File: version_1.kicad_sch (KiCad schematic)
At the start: 2 parts, among them U1 74AHC595, U10 74AHC595

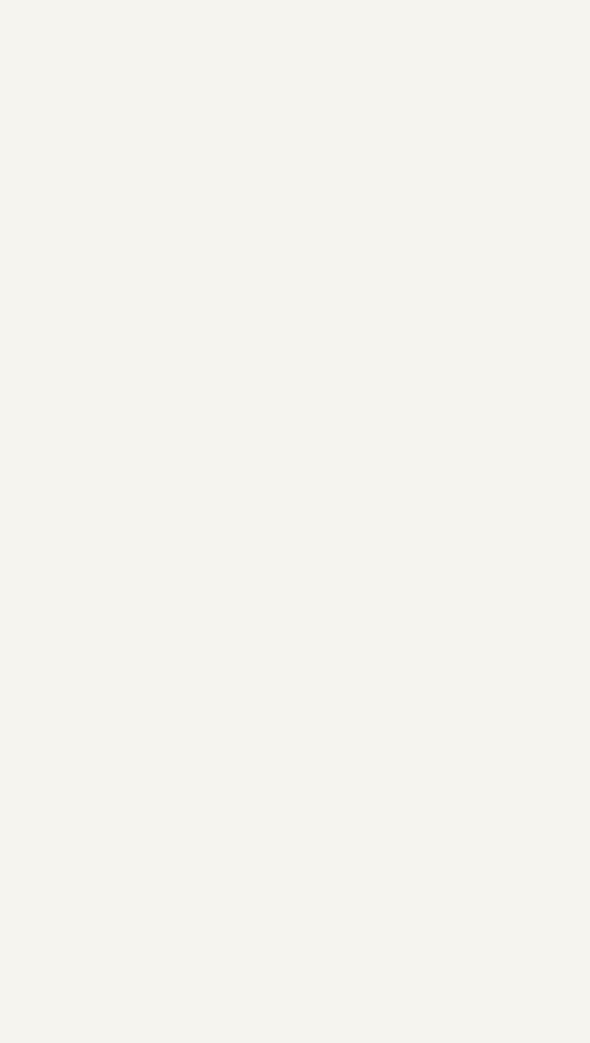
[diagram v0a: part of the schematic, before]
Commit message: mostek H, serva, SMPS
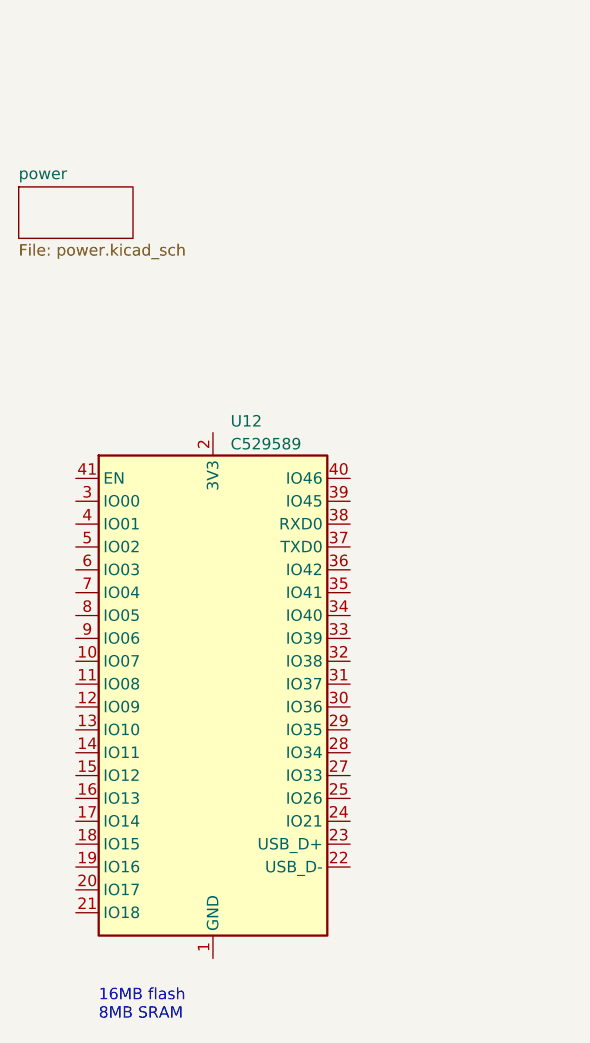
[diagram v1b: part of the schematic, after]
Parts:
- added U12: C529589, RF_Module:ESP32-S2-WROVER, symbol RF_Module:ESP32-S2-WROVER
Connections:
- new net: U12.1 (GND), U12.26 (GND), U12.42 (GND), U12.43 (GND)
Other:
- added sheet power (power.kicad_sch)
- note added: "16MB flash 8MB SRAM"
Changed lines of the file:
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@@
     (stroke (width 0) (type default))
+  )
+  (text "16MB flash\n8MB SRAM" (at 76.835 146.685 0)
+    (effects (font (size 1.27 1.27)) (justify left bottom))
   )
   (symbol (lib_id "power:+5V") (at 226.06 26.035 0) (unit 1)
@@
     )
   )
+  (symbol (lib_id "RF_Module:ESP32-S2-WROVER") (at 89.535 111.76 0) (unit 1)
+    (in_bom yes) (on_board yes) (dnp no) (fields_autoplaced)
+    (property "Reference" "U12" (at 91.4909 80.01 0)
+      (effects (font (size 1.27 1.27)) (justify left))
+    )
+    (property "Value" "C529589" (at 91.4909 82.55 0)
+      (effects (font (size 1.27 1.27)) (justify left))
+    )
+    (property "Footprint" "RF_Module:ESP32-S2-WROVER" (at 108.585 140.97 0)
+      (effects (font (size 1.27 1.27)) hide)
+    )
+    (property "Datasheet" "https://www.espressif.com/sites/default/files/documentation/esp32-s2-wroom_esp32-s2-wroom-i_datasheet_en.pdf" (at 81.915 132.08 0)
+      (effects (font (size 1.27 1.27)) hide)
+    )
+    (pin "1")
+    (pin "10")
+    (pin "11")
+    (pin "12")
+    (pin "13")
+    (pin "14")
+    (pin "15")
+    (pin "16")
+    (pin "17")
+    (pin "18")
+    (pin "19")
+    (pin "2")
+    (pin "20")
+    (pin "21")
+    (pin "22")
+    (pin "23")
+    (pin "24")
+    (pin "25")
+    (pin "26")
+    (pin "27")
+    (pin "28")
+    (pin "29")
+    (pin "3")
+    (pin "30")
+    (pin "31")
+    (pin "32")
+    (pin "33")
+    (pin "34")
+    (pin "35")
+    (pin "36")
+    (pin "37")
+    (pin "38")
+    (pin "39")
+    (pin "4")
+    (pin "40")
+    (pin "41")
+    (pin "42")
+    (pin "43")
+    (pin "5")
+    (pin "6")
+    (pin "7")
+    (pin "8")
+    (pin "9")
+    (instances
+      (project "version_1"
+        (path "/23ba0750-4a55-4d50-828b-749cc0fbb8c8"
+          (reference "U12") (unit 1)
+        )
+      )
+    )
+  )
   (symbol (lib_id "power:+5V") (at 214.63 38.735 0) (unit 1)
     (in_bom yes) (on_board yes) (dnp no) (fields_autoplaced)
@@
       )
     )
+  )
+  (sheet (at 67.945 53.975) (size 12.7 5.715) (fields_autoplaced)
+    (stroke (width 0.1524) (type solid))
+    (fill (color 0 0 0 0.0000))
+    (property "Sheetname" "power" (at 67.945 53.2634 0)
+      (effects (font (size 1.27 1.27)) (justify left bottom))
+    )
+    (property "Sheetfile" "power.kicad_sch" (at 67.945 60.2746 0)
+      (effects (font (size 1.27 1.27)) (justify left top))
+    )
+    (property "Field2" "" (at 67.945 53.975 0)
+      (effects (font (size 1.27 1.27)) hide)
+    )
+    (instances
+      (project "version_1"
+        (path "/23ba0750-4a55-4d50-828b-749cc0fbb8c8" (page "10"))
+      )
+    )

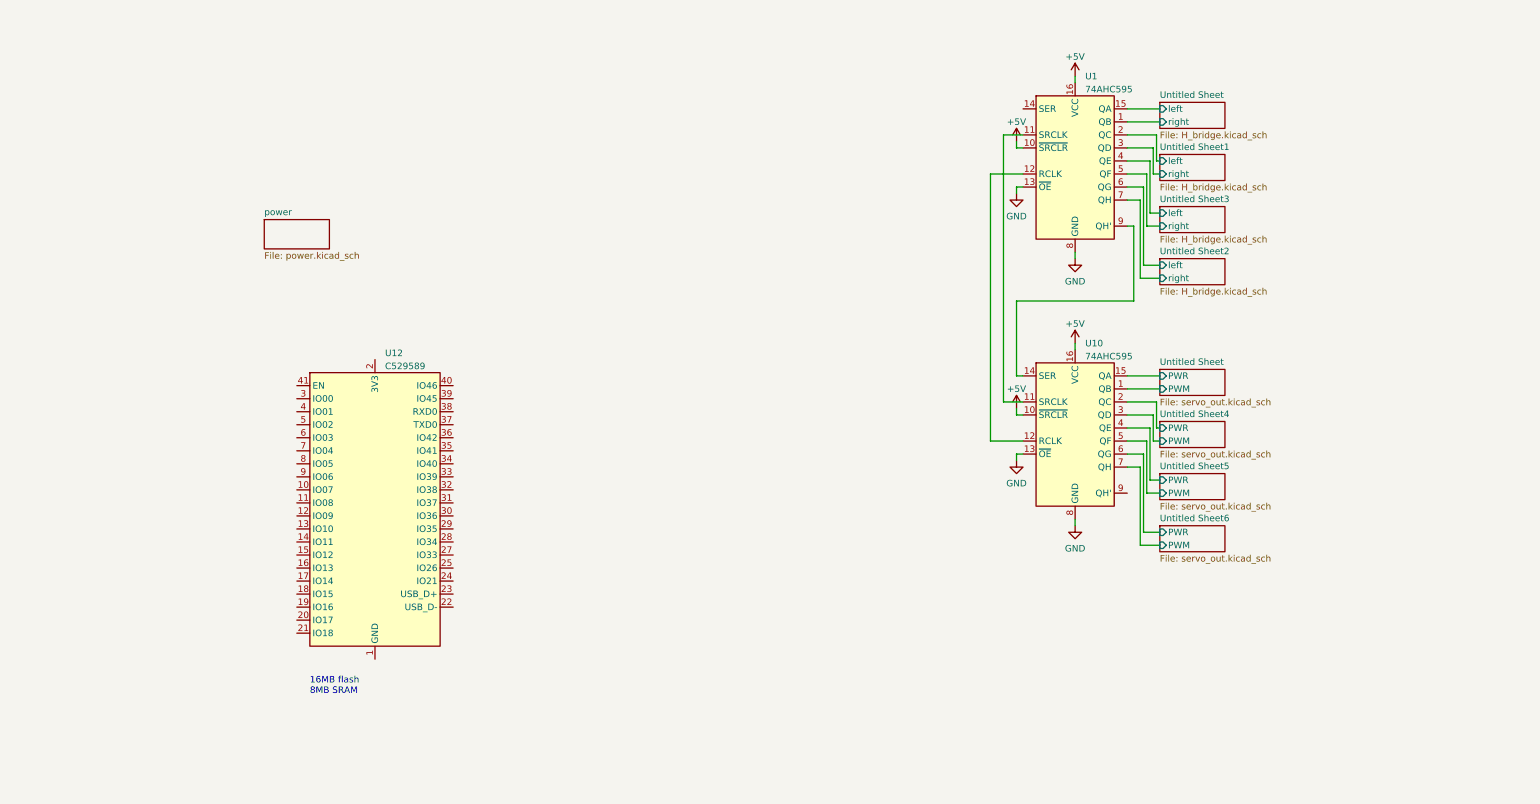
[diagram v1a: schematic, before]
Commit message: routing of H bridges and servo power pins
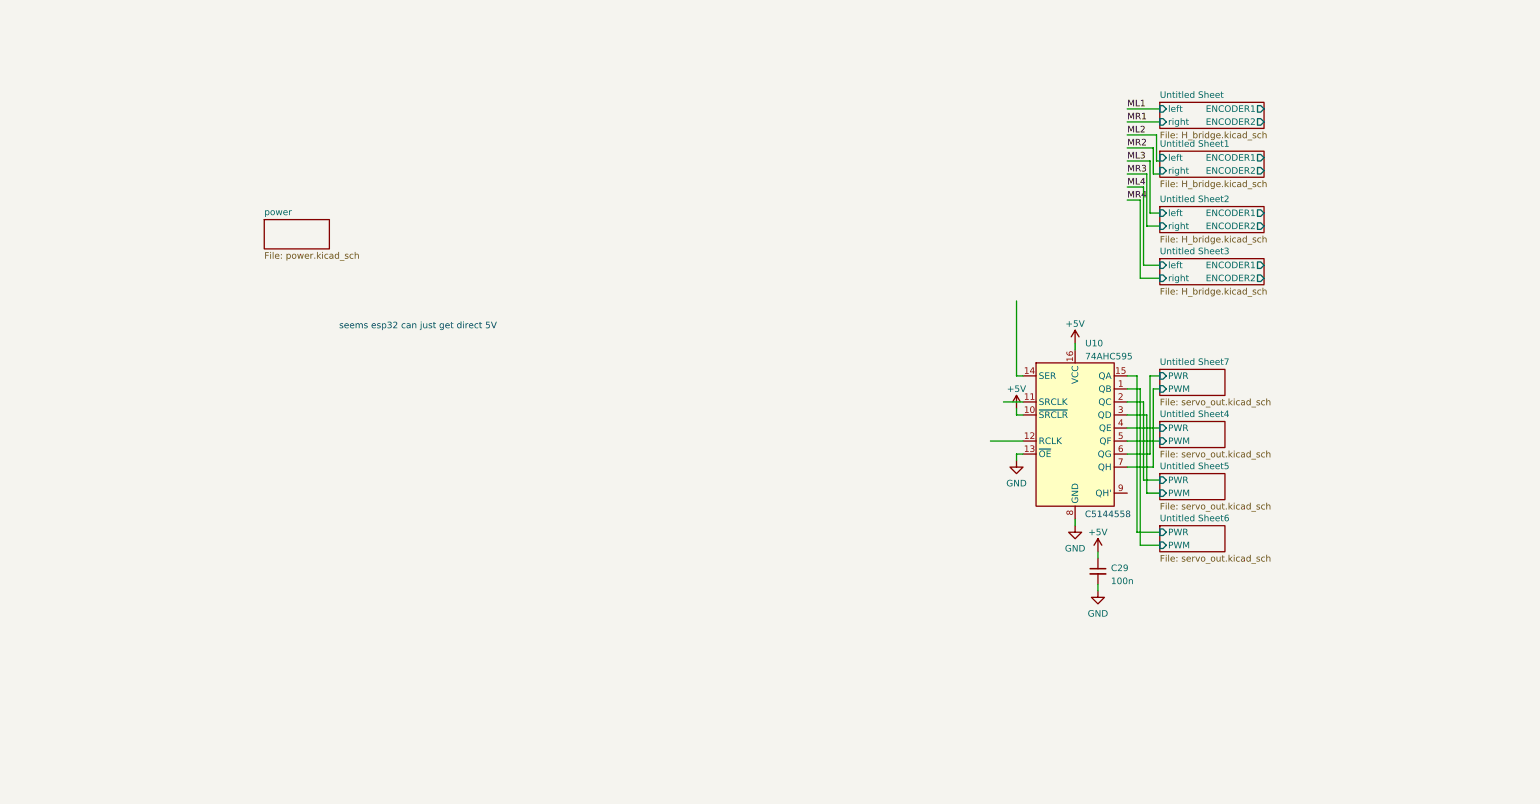
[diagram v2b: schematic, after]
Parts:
- removed U1: 74AHC595, symbol 74xx:74AHC595
- removed U12: C529589, RF_Module:ESP32-S2-WROVER, symbol RF_Module:ESP32-S2-WROVER
- added C29: 100n, Capacitor_SMD:C_0603_1608Metric_Pad1.08x0.95mm_HandSolder, symbol Device:C_Small
- U10: footprint (none) -> Package_SO:SOP-16_3.9x9.9mm_P1.27mm
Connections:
- net Untitled Sheet/PWM is gone; now on net Untitled Sheet6/PWM: U10.1 (QB)
- net Untitled Sheet/PWR is gone; now on net Untitled Sheet6/PWR: U10.15 (QA)
- net +5V: now also C29.1
- net GND: now also C29.2
- net Untitled Sheet4/PWM: now also U10.5 (QF); no longer U10.3 (QD)
- net Untitled Sheet4/PWR: now also U10.4 (QE); no longer U10.2 (QC)
- net Untitled Sheet5/PWM: now also U10.3 (QD); no longer U10.5 (QF)
- net Untitled Sheet5/PWR: now also U10.2 (QC); no longer U10.4 (QE)
- net Untitled Sheet6/PWM: no longer U10.7 (QH)
- net Untitled Sheet6/PWR: no longer U10.6 (QG)
- new net Untitled Sheet7/PWM: U10.7 (QH)
- new net Untitled Sheet7/PWR: U10.6 (QG)
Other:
- added sheet Untitled Sheet7 (servo_out.kicad_sch)
- sheet Untitled Sheet: file servo_out.kicad_sch -> H_bridge.kicad_sch
- sheet Untitled Sheet ports: added ENCODER1, ENCODER2, left, right; removed PWM, PWR
- sheet Untitled Sheet1 ports: added ENCODER1, ENCODER2; removed none
- sheet Untitled Sheet2 ports: added ENCODER1, ENCODER2; removed none
- sheet Untitled Sheet3 ports: added ENCODER1, ENCODER2; removed none
- note added: "C5144558"
- note added: "seems esp32 can just get direct 5V"
- note removed: "16MB flash 8MB SRAM"

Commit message: more capacitance near motors 16x22uF total 3S->2S
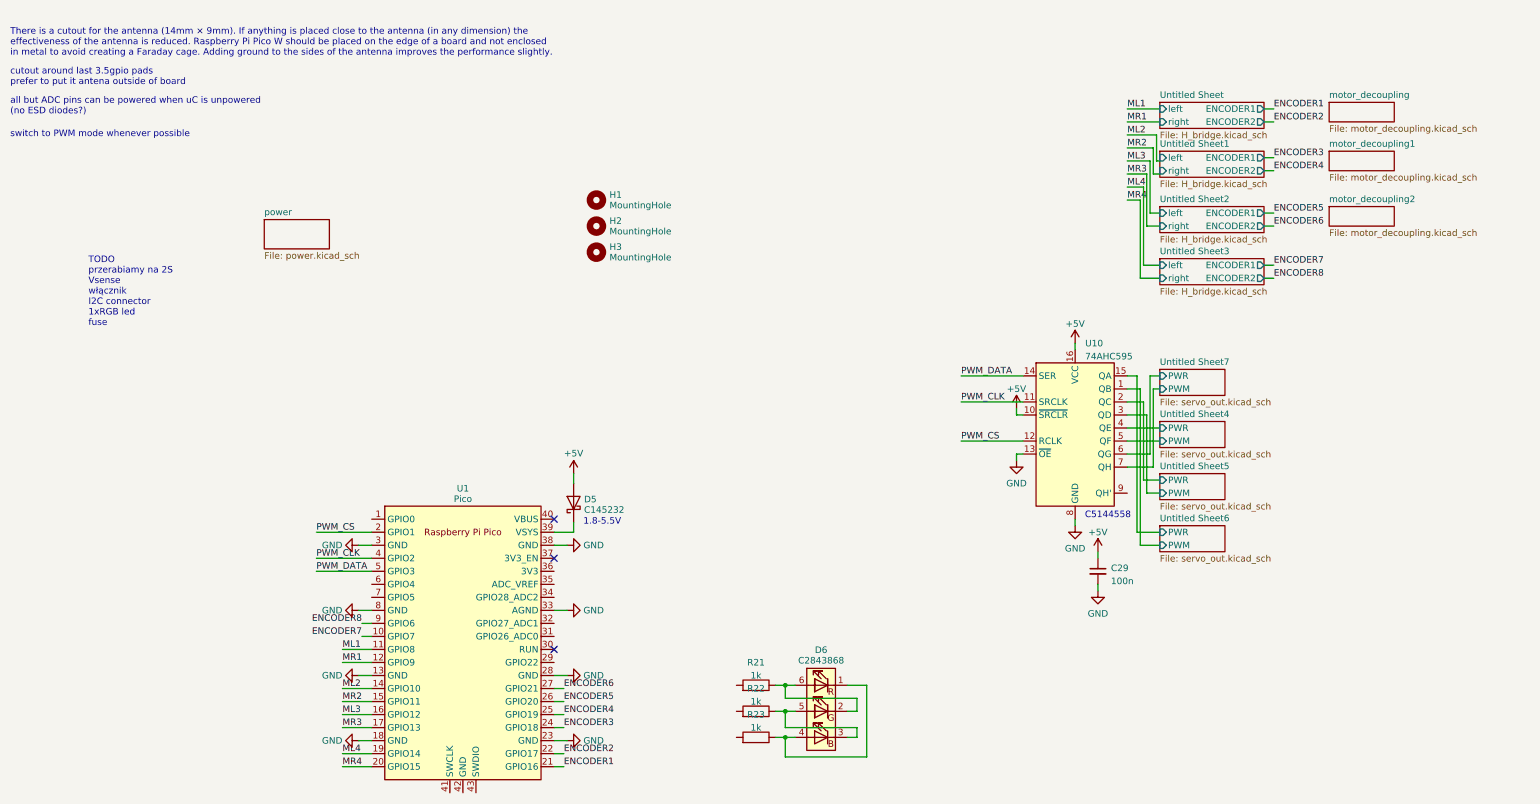
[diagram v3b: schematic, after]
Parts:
- added D5: C145232, Diode_SMD:D_SMA_Handsoldering, symbol Device:D_Schottky
- added D6: C2843868, LED_SMD:LED_RGB_5050-6, symbol Device:LED_RGB
- added H1, H2, H3: MountingHole, MountingHole:MountingHole_3.2mm_M3, symbol Mechanical:MountingHole
- added R21, R22, R23: 1k, Resistor_SMD:R_0603_1608Metric_Pad0.98x0.95mm_HandSolder, symbol Device:R
- added U1: Pico, MCU_RaspberryPi_and_Boards:RPi_Pico_SMD_TH, symbol MCU_RaspberryPi_and_Boards:Pico
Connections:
- net +5V: now also D5.2 (A)
- net GND: now also U1.13 (GND), U1.18 (GND), U1.23 (GND), U1.28 (GND), U1.3 (GND), U1.33 (AGND), U1.38 (GND), U1.8 (GND)
- net ML1: now also U1.11 (GPIO8)
- net ML2: now also U1.14 (GPIO10)
- net ML3: now also U1.16 (GPIO12)
- net ML4: now also U1.19 (GPIO14)
- net MR1: now also U1.12 (GPIO9)
- net MR2: now also U1.15 (GPIO11)
- net MR3: now also U1.17 (GPIO13)
- net MR4: now also U1.20 (GPIO15)
- net PWM_CLK: now reaches U10.11 (SRCLK)
- net PWM_CLK: now also U1.4 (GPIO2)
- net PWM_CS: now reaches U10.12 (RCLK)
- net PWM_CS: now also U1.2 (GPIO1)
- net PWM_DATA: now reaches U10.14 (SER)
- net PWM_DATA: now also U1.5 (GPIO3)
- new net: D6.1 (RK), D6.4 (BA), R23.1
- new net: D6.2 (GK), D6.6 (RA), R21.1
- new net: D6.3 (BK), D6.5 (GA), R22.1
- new net: D5.1 (K), U1.39 (VSYS)
- new net ENCODER1: U1.21 (GPIO16)
- new net ENCODER2: U1.22 (GPIO17)
- new net ENCODER3: U1.24 (GPIO18)
- new net ENCODER4: U1.25 (GPIO19)
- new net ENCODER5: U1.26 (GPIO20)
- new net ENCODER6: U1.27 (GPIO21)
- new net ENCODER7: U1.10 (GPIO7)
- new net ENCODER8: U1.9 (GPIO6)
- no-connect marks 0 -> 3
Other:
- added sheet motor_decoupling (motor_decoupling.kicad_sch)
- added sheet motor_decoupling1 (motor_decoupling.kicad_sch)
- added sheet motor_decoupling2 (motor_decoupling.kicad_sch)
- note added: "1.8-5.5V"
- note added: "TODO przerabiamy na 2S Vsense włącznik I2C connector 1xRGB led fuse"
- note added: "There is a cutout for the antenna (14mm × 9mm). If anything is placed close to the antenna (in any dimension) the effectiveness of the antenna is reduced. Raspberry Pi Pico W should be placed on the edge of a board and not enclosed in metal to avoid creating a Faraday cage. Adding ground to the sides of the antenna improves the performance slightly."
- note added: "all but ADC pins can be powered when uC is unpowered (no ESD diodes?)"
- note added: "cutout around last 3.5gpio pads prefer to put it antena outside of board"
- note added: "switch to PWM mode whenever possible"
- note removed: "seems esp32 can just get direct 5V"

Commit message: verison 1.0 just routed
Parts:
- added C15: 22u, Capacitor_SMD:C_0805_2012Metric_Pad1.18x1.45mm_HandSolder, symbol Device:C
- added C16: 100n, Capacitor_SMD:C_0603_1608Metric_Pad1.08x0.95mm_HandSolder, symbol Device:C_Small
- added R25, R26, R27: 1k, Resistor_SMD:R_0603_1608Metric_Pad0.98x0.95mm_HandSolder, symbol Device:R
- added U12: LSM6DS3, Package_LGA:LGA-14_3x2.5mm_P0.5mm_LayoutBorder3x4y, symbol Sensor_Motion:LSM6DS3
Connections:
- net +5V: now also C16.1
- net ENCODER1: now also U1.14 (GPIO10); no longer U1.21 (GPIO16)
- net ENCODER2: now also U1.15 (GPIO11); no longer U1.22 (GPIO17)
- net ENCODER3: now also U1.16 (GPIO12); no longer U1.24 (GPIO18)
- net ENCODER4: now also U1.17 (GPIO13); no longer U1.25 (GPIO19)
- net ENCODER5: now also U1.19 (GPIO14); no longer U1.26 (GPIO20)
- net ENCODER6: now also U1.20 (GPIO15); no longer U1.27 (GPIO21)
- net ENCODER7: now also U1.29 (GPIO22); no longer U1.10 (GPIO7)
- net ENCODER8: now also U1.12 (GPIO9); no longer U1.9 (GPIO6)
- net GND: now also C15.2, C16.2, R25.1
- net ML1: now also U1.27 (GPIO21); no longer U1.11 (GPIO8)
- net ML2: now also U1.25 (GPIO19); no longer U1.14 (GPIO10)
- net ML3: now also U1.22 (GPIO17); no longer U1.16 (GPIO12)
- net ML4: now also U1.32 (GPIO27_ADC1); no longer U1.19 (GPIO14)
- net MR1: now also U1.26 (GPIO20); no longer U1.12 (GPIO9)
- net MR2: now also U1.24 (GPIO18); no longer U1.15 (GPIO11)
- net MR3: now also U1.21 (GPIO16); no longer U1.17 (GPIO13)
- net MR4: now also U1.31 (GPIO26_ADC0); no longer U1.20 (GPIO15)
- net PWM_CLK: now also U1.9 (GPIO6); no longer U1.4 (GPIO2)
- net PWM_CS: now also U1.7 (GPIO5); no longer U1.2 (GPIO1)
- net PWM_DATA: now also U1.10 (GPIO7); no longer U1.5 (GPIO3)
- net at R23.2: now also U1.4 (GPIO2)
- net at U1.1 (GPIO0): now also R21.2
- net at U1.34 (GPIO28_ADC2): now also C15.1, R25.2, R26.2
- net +3.3V: now reaches U1.36 (3V3)
- net at R22.2: now also U1.2 (GPIO1)
- new net: R26.1, R27.2
- new net: U12.6 (GND), U12.7 (GND)
- new net VCC: R27.1
- no-connect marks 3 -> 4
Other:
- note added: "3.3V max"
- note added: "TODO I2C connector I2C ACC vs Pgood form SMPS?"
- note added: "motor 4 - PWM 5 motor 1 - PWM 2 motor 2 - PWM 1 motor 3 - PWM 0"
- note removed: "TODO przerabiamy na 2S Vsense włącznik I2C connector 1xRGB led fuse"
- moved on the sheet: D6, R21, R22, R23
